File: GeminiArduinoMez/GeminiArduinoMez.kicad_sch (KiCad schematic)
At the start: 9 parts, among them J1 Conn_02x10_Odd_Even, J2 Conn_01x02, J3 Conn_01x05, SW1 TACT_SW

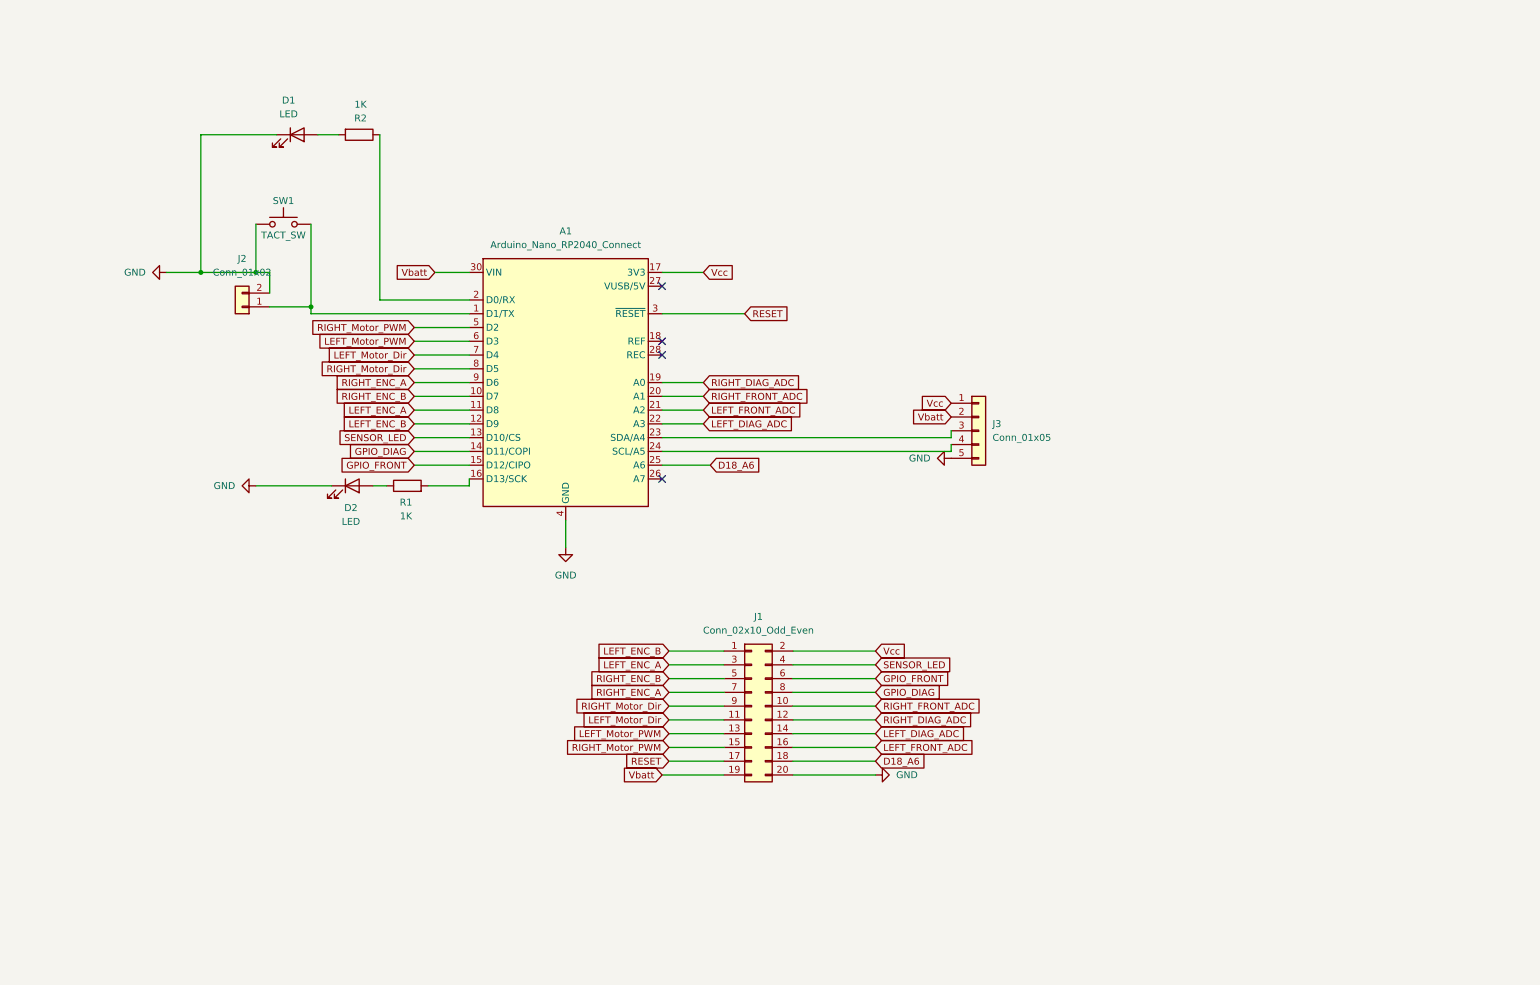
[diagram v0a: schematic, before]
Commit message: Version 2 of boards sent to JLCPCB and a new calibration board
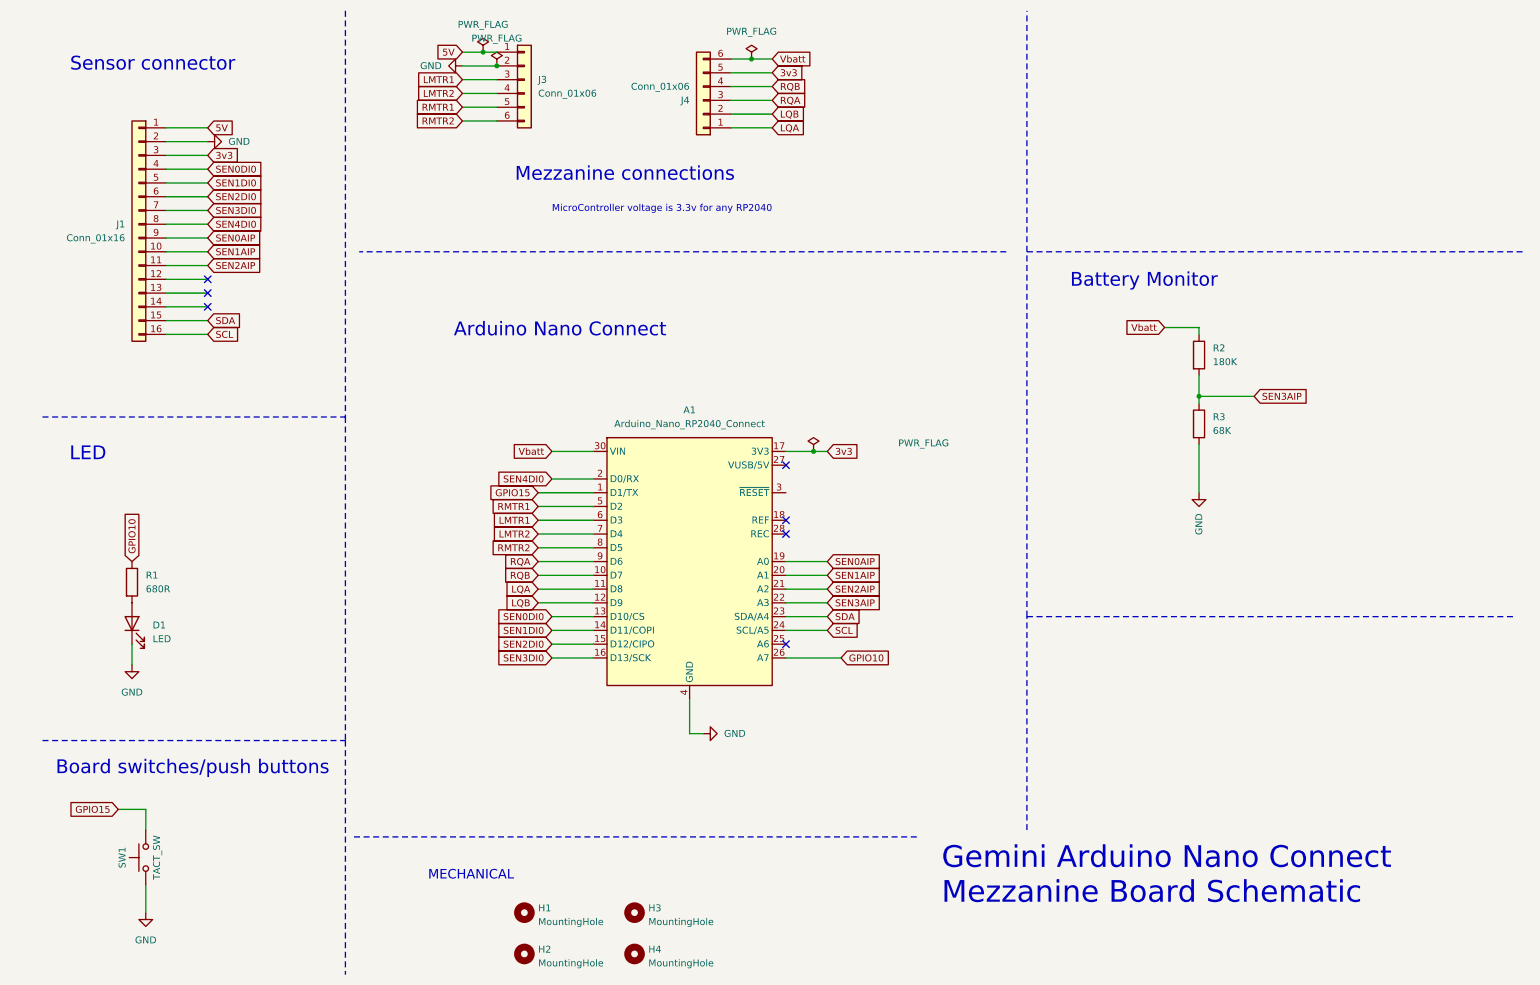
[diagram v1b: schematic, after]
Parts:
- removed D2: LED, LED_THT:LED_D5.0mm, symbol Device:LED
- removed J1: Conn_02x10_Odd_Even, Connector_PinHeader_2.54mm:PinHeader_2x10_P2.54mm_Horizontal, symbol Connector_Generic:Conn_02x10_Odd_Even
- removed J2: Conn_01x02, Connector_PinHeader_2.54mm:PinHeader_1x02_P2.54mm_Vertical, symbol Connector_Generic:Conn_01x02
- removed J3: Conn_01x05, Connector_PinSocket_2.54mm:PinSocket_1x05_P2.54mm_Vertical, symbol Connector_Generic:Conn_01x05
- added H1, H2, H3, H4: MountingHole, ukmarsbot:MountingHole_3.2mm_M3_clearance, symbol Mechanical:MountingHole
- added J1: Conn_01x16, Connector_PinHeader_2.54mm:PinHeader_1x16_P2.54mm_Vertical, symbol Connector_Generic:Conn_01x16
- added J3, J4: Conn_01x06, Connector_PinHeader_2.54mm:PinHeader_1x06_P2.54mm_Vertical, symbol Connector_Generic:Conn_01x06
- added R3: 68K, Resistor_THT:R_Axial_DIN0207_L6.3mm_D2.5mm_P7.62mm_Horizontal, symbol Device:R
- R1: value 1K -> 680R
- R2: value 1K -> 180K
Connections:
- net GND: now also J1.2 (Pin_2), J3.2 (Pin_2), R3.2
- net Vbatt: now also R2.1, J4.6 (Pin_6)
- net GPIO10: now reaches R1.1
- net GPIO10: now also A1.26 (A7)
- net GPIO15: now reaches A1.1 (D1/TX), SW1.2 (B)
- net SEN4DI0: now reaches A1.2 (D0/RX)
- net SEN4DI0: now also J1.8 (Pin_8); no longer R2.1
- net at D1.2 (A): now also R1.2; no longer R2.2
- net SEN3DI0: now reaches A1.16 (D13/SCK)
- net SEN3DI0: now also J1.7 (Pin_7); no longer R1.2
- net SDA: now reaches A1.23 (SDA/A4)
- net SDA: now also J1.15 (Pin_15)
- net SCL: now reaches A1.24 (SCL/A5)
- net SCL: now also J1.16 (Pin_16)
- net D18_A6: no longer names the net of A1.25 (A6)
- net GPIO_DIAG renamed SEN1DI0
- net SEN1DI0: now also J1.5 (Pin_5)
- net GPIO_FRONT renamed SEN2DI0
- net SEN2DI0: now also J1.6 (Pin_6)
- net LEFT_DIAG_ADC renamed SEN3AIP
- net SEN3AIP: now also R2.2, R3.1
- net LEFT_ENC_A renamed LQA
- net LQA: now also J4.1 (Pin_1)
- net LEFT_ENC_B renamed LQB
- net LQB: now also J4.2 (Pin_2)
- net LEFT_FRONT_ADC renamed SEN2AIP
- net SEN2AIP: now also J1.11 (Pin_11)
- net LEFT_Motor_Dir renamed LMTR2
- net LMTR2: now also J3.4 (Pin_4)
- net LEFT_Motor_PWM renamed LMTR1
- net LMTR1: now also J3.3 (Pin_3)
- net RESET: no longer names the net of A1.3 (~{RESET})
- net RIGHT_DIAG_ADC renamed SEN0AIP
- net SEN0AIP: now also J1.9 (Pin_9)
- net RIGHT_ENC_A renamed RQA
- net RQA: now also J4.3 (Pin_3)
- net RIGHT_ENC_B renamed RQB
- net RQB: now also J4.4 (Pin_4)
- net RIGHT_FRONT_ADC renamed SEN1AIP
- net SEN1AIP: now also J1.10 (Pin_10)
- net RIGHT_Motor_Dir renamed RMTR2
- net RMTR2: now also J3.6 (Pin_6)
- net RIGHT_Motor_PWM renamed RMTR1
- net RMTR1: now also J3.5 (Pin_5)
- net SENSOR_LED renamed SEN0DI0
- net SEN0DI0: now also J1.4 (Pin_4)
- net Vcc renamed 3v3
- net 3v3: now also J1.3 (Pin_3), J4.5 (Pin_5)
- new net 5V: J1.1 (Pin_1), J3.1 (Pin_1)
- no-connect marks 4 -> 7
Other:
- note added: "Arduino Nano Connect"
- note added: "Battery Monitor"
- note added: "Board switches/push buttons"
- note added: "Gemini Arduino Nano Connect Mezzanine Board Schematic"
- note added: "LED"
- note added: "MECHANICAL"
- note added: "Mezzanine connections"
- note added: "MicroController voltage is 3.3v for any RP2040"
- note added: "Sensor connector"
- title: Carrier Board for the Ardunio Nano RP2040 Connect -> Gemini Arduino Nano Connect Mezzanine
